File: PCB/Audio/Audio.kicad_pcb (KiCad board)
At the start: 2 copper layers, 70 x 70 mm, 36 parts, among them J1 JST-PH-SM4-TB, J3 TC2030-USB-NL-DS, J4 TF_PUSH, J5 USB-C-Socket-H, Q2 CJ2301, SW1 SW_Push, U1 R, U2 L, U3 TP4054, U4 ME6211C33M5G-N, U6 ESP32-S3-MINI-1

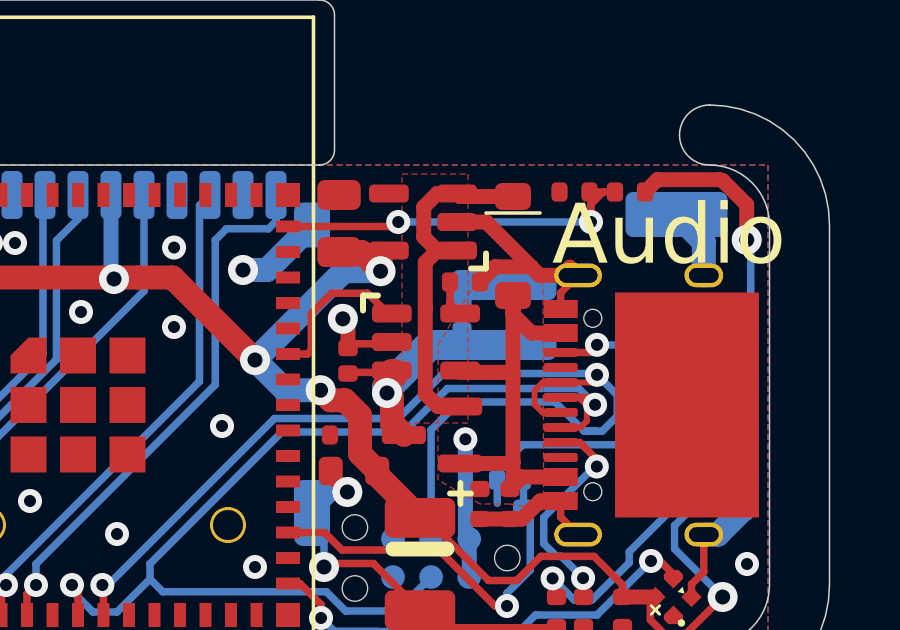
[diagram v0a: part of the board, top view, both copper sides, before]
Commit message: Cap clash moved
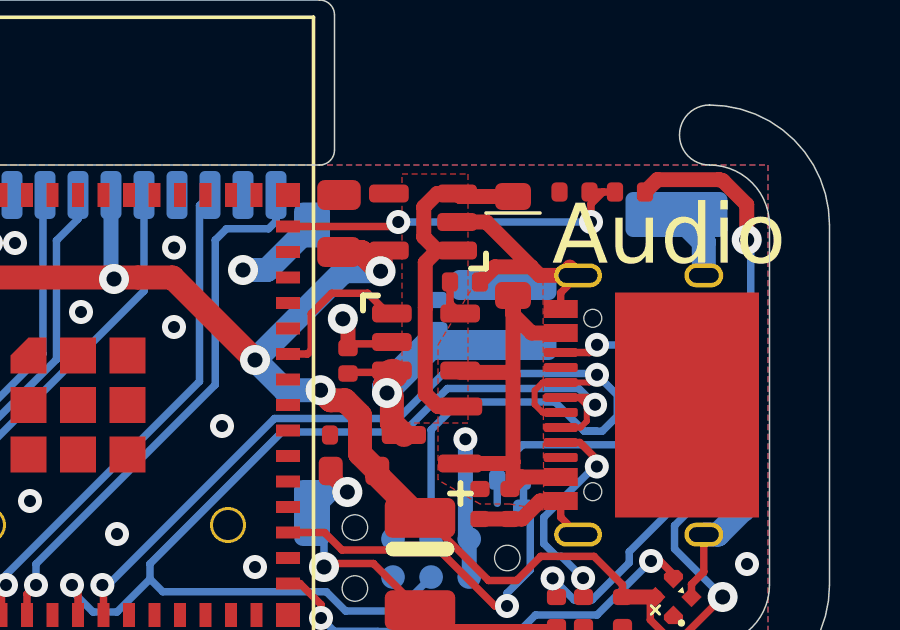
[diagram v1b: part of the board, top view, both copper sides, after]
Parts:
- moved C7 0.80 mm to (112.0, 97.0)

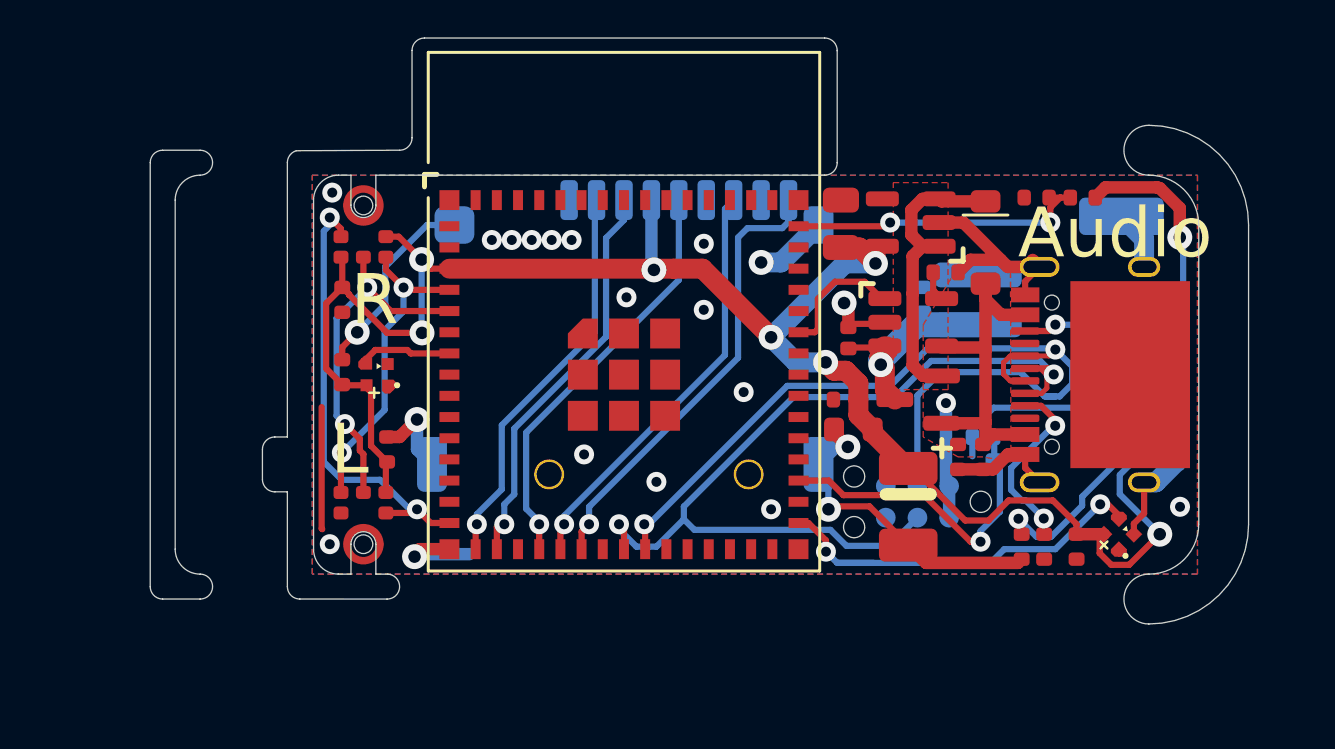
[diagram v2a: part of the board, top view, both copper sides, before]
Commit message: Rework, and pull ups
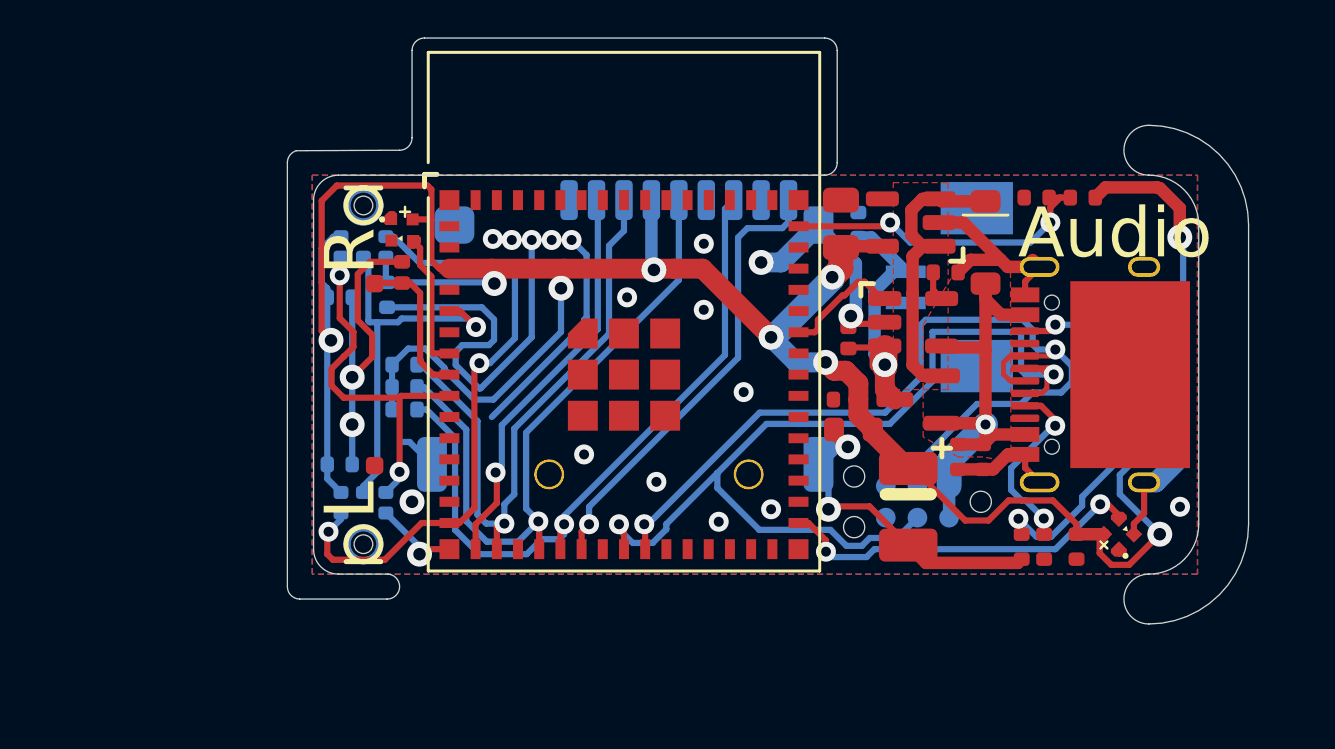
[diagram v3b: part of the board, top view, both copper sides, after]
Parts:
- added R3: 10K, RevK:R_0402, B.Cu at (91.2, 100.5)
- added R4: 10K, RevK:R_0402, B.Cu at (91.2, 99.6)
- added R7: 10K, RevK:R_0402, B.Cu at (91.2, 101.4)
- C13, C6, C8, U1, U2: moved to B.Cu
- D4, SW1: moved to F.Cu
- J1: value JST-PH-SM4-TB -> Battery; footprint RevK:JST_PH_S2B-PH-SM4-TB_1x02-1MP_P2.00mm_Horizontal -> RevK:1.25T-2PWT (Molex 532610271)
- moved SW1 28.7 mm to (90.0, 100.0), turned to 90 degrees
- moved D4 24.2 mm to (91.1, 95.9), turned to 90 degrees
- moved D5 5.89 mm to (91.1, 94.2), turned to 0 degrees
- moved C7 3.97 mm to (109.4, 94.0)
- moved C6 3.58 mm to (90.5, 96.8), turned to -90 degrees
- moved J1 2.89 mm to (114.2, 96.5), turned to 90 degrees
- moved C13 1.99 mm to (88.6, 103.6), turned to 180 degrees
- moved C8 0.14 mm to (88.6, 96.9), turned to 180 degrees
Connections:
- U6 pad 33: BUTTON -> unconnected-(U6-GPIO37-Pad33)
- U6 pad 4: WS -> unconnected-(U6-GPIO0-Pad4)
- U6 pad 8: unconnected-(U6-GPIO4-Pad8) -> BUTTON
- U6 pad 9: unconnected-(U6-GPIO5-Pad9) -> WS
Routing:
- net +3V3: track 97.9 -> 118.9 mm, vias 8 -> 9
- net GND: track 64.8 -> 81.3 mm
- net SDMISO: track 16.9 -> 28.1 mm
- net SDSCK: track 16.8 -> 26.7 mm
- net SDMOSI: track 16.0 -> 24.3 mm
- net SCK: track 17.9 -> 24.8 mm
- net BUTTON: track 12.9 -> 6.14 mm, vias 1 -> 0
- net VBAT: track 9.35 -> 11.8 mm
- net D-: track 36.6 -> 39.1 mm
- net WS: track 12.6 -> 14.8 mm
- net D+: track 38.7 -> 36.7 mm
- net BLINK2: track 3.68 -> 5.52 mm
- net BLINK: track 16.3 -> 14.7 mm
- net SD: track 14.1 -> 15.6 mm, vias 2 -> 1
- net VBUS: track 19.1 -> 19.7 mm
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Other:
- board text added: "+"
- board text added: "-"
- board text added: "BA"
- board text removed: "A"

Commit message: Placement
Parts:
- moved J1 1.75 mm to (112.5, 96.5)
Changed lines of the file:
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@@
 		(fp_arc
 			(start 0.27561 0.422802)
-			(mid 0.162324 0.224752)
+			(mid 0.162323 0.224752)
 			(end 0.123007 0.000003)
 			(stroke
@@
 		(fp_arc
 			(start 0.362198 -0.50939)
-			(mid 0.560248 -0.622677)
+			(mid 0.560248 -0.622676)
 			(end 0.784997 -0.661993)
 			(stroke
@@
 		(fp_arc
 			(start 0.362198 -0.50939)
-			(mid 0.560248 -0.622677)
+			(mid 0.560248 -0.622676)
 			(end 0.784997 -0.661993)
 			(stroke
@@
 		(fp_arc
 			(start 0.27561 0.422802)
-			(mid 0.162324 0.224752)
+			(mid 0.162323 0.224752)
 			(end 0.123007 0.000003)
 			(stroke
@@
 	(footprint "RevK:1.25T-2PWT (Molex 532610271)"
 		(layer "B.Cu")
-		(at 114.2 96.5 90)
+		(at 112.45 96.5 90)
 		(property "Reference" "J1"
 			(at 0 0 -90)
@@
 		(attr smd)
 		(pad "" smd rect
-			(at -3.157 -0.05 90)
+			(at -3.157 1.7 90)
 			(size 2.1 2.9)
 			(layers "B.Cu" "B.Paste" "B.Mask")
-			(teardrops
-				(best_length_ratio 0.5)
-				(max_length 1)
-				(best_width_ratio 1)
-				(max_width 2)
-				(curve_points 5)
-				(filter_ratio 0.9)
-				(enabled yes)
-				(allow_two_segments yes)
-				(prefer_zone_connections no)
-			)
 		)
 		(pad "" smd rect
-			(at 3.175 -0.05 90)
+			(at 3.175 1.7 90)
 			(size 2.1 2.9)
 			(layers "B.Cu" "B.Paste" "B.Mask")
-			(teardrops
-				(best_length_ratio 0.5)
-				(max_length 1)
-				(best_width_ratio 1)
-				(max_width 2)
-				(curve_points 5)
-				(filter_ratio 0.9)
-				(enabled yes)
-				(allow_two_segments yes)
-				(prefer_zone_connections no)
-			)
 		)
 		(pad "1" smd rect
-			(at -0.625 -2.9 90)
+			(at -0.625 -1.15 90)
 			(size 0.5 1.6)
 			(layers "B.Cu" "B.Paste" "B.Mask")
@@
 			(pinfunction "Pin_1")
 			(pintype "passive")
-			(teardrops
-				(best_length_ratio 0.5)
-				(max_length 1)
-				(best_width_ratio 1)
-				(max_width 2)
-				(curve_points 5)
-				(filter_ratio 0.9)
-				(enabled yes)
-				(allow_two_segments yes)
-				(prefer_zone_connections no)
-			)
 		)
 		(pad "2" smd rect
-			(at 0.625 -2.9 90)
+			(at 0.625 -1.15 90)
 			(size 0.5 1.6)
 			(layers "B.Cu" "B.Paste" "B.Mask")
@@
 			(pinfunction "Pin_2")
 			(pintype "passive")
-			(teardrops
-				(best_length_ratio 0.5)
-				(max_length 1)
-				(best_width_ratio 1)
-				(max_width 2)
-				(curve_points 5)
-				(filter_ratio 0.9)
-				(enabled yes)
-				(allow_two_segments yes)
-				(prefer_zone_connections no)
-			)
 		)
 		(model "${KISYS3DMOD}/Connector_Molex.3dshapes/Molex_PicoBlade_53261-0271_1x02-1MP_P1.25mm_Horizontal.step"
 			(offset
-				(xyz 0 -0.5 0)
+				(xyz 0 1.5 0)
 			)
 			(scale

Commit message: Resistors
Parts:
- removed R3, R4, R7: 10K, RevK:R_0402
- added R10: 10K, RevK:R_0402, B.Cu at (91.2, 101.8)
- added R11: 10K, RevK:R_0402, B.Cu at (91.2, 100.9)
- added R12: 10K, RevK:R_0402, B.Cu at (91.2, 100.0)
- added R13: 10K, RevK:R_0402, B.Cu at (91.2, 99.1)
- added R14: 10K, RevK:R_0402, B.Cu at (96.2, 92.7)
- added R9: 10K, RevK:R_0402, B.Cu at (108.8, 100.7)
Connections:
- J4 pad 1: unconnected-(J4-DAT2-Pad1) -> Net-(J4-DAT2)
- J4 pad 8: unconnected-(J4-DAT1-Pad8) -> Net-(J4-DAT1)
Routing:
- net Net-(J4-DAT1): track 0.00 -> 29.8 mm
- net GND: track 81.3 -> 68.8 mm, vias 22 -> 20
- net SDSS: track 16.1 -> 21.1 mm
- net +3V3: track 118.9 -> 123.6 mm, vias 9 -> 10
- net SDMISO: track 28.1 -> 30.2 mm
- net Net-(J4-DAT2): track 0.00 -> 1.18 mm

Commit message: Reworked
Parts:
- moved R9 17.6 mm to (91.2, 101.9), turned to 0 degrees
- moved D5 7.72 mm to (86.0, 100.0)
- moved C13 1.72 mm to (87.6, 102.2), turned to -90 degrees
- moved C8 1.28 mm to (87.6, 97.7), turned to 90 degrees
- moved U2 1.08 mm to (89.4, 104.9), turned to -45 degrees
- moved U1 1.06 mm to (89.4, 95.1), turned to 45 degrees
- moved C6 0.92 mm to (91.2, 97.4), turned to 0 degrees
- moved R11 0.80 mm to (91.2, 100.1)
- moved R10 0.80 mm to (91.2, 101.0)
- moved R12 0.80 mm to (91.2, 99.2)
- moved R13 0.80 mm to (91.2, 98.3)
- moved D4 0.14 mm to (91.0, 96.0), turned to -90 degrees
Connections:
- U6 pad 10: unconnected-(U6-GPIO6-Pad10) -> WS
- U6 pad 11: unconnected-(U6-GPIO7-Pad11) -> SD
- U6 pad 12: unconnected-(U6-GPIO8-Pad12) -> GND
- U6 pad 13: unconnected-(U6-GPIO9-Pad13) -> BLINK2
- U6 pad 14: unconnected-(U6-GPIO10-Pad14) -> SCK
- U6 pad 15: SCK -> GND
- U6 pad 22: unconnected-(U6-GPIO18-Pad22) -> CHARGING
- U6 pad 5: SD -> BUTTON
- U6 pad 6: unconnected-(U6-GPIO2-Pad6) -> GND
- U6 pad 7: BLINK2 -> unconnected-(U6-GPIO3-Pad7)
- U6 pad 8: BUTTON -> unconnected-(U6-GPIO4-Pad8)
- U6 pad 9: WS -> unconnected-(U6-GPIO5-Pad9)
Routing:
- net CHARGING: track 4.75 -> 19.0 mm
- net SCK: track 24.6 -> 30.2 mm
- net BLINK2: track 5.52 -> 10.5 mm
- net +3V3: track 123.6 -> 119.0 mm, vias 10 -> 8
- net GND: track 68.8 -> 72.4 mm, vias 20 -> 23
- net WS: track 14.8 -> 16.8 mm, vias 2 -> 1
- net BUTTON: track 6.11 -> 4.45 mm
- net SDSS: track 21.1 -> 22.3 mm
- net SDMISO: track 30.2 -> 31.3 mm
- net SDSCK: track 26.3 -> 27.4 mm
- net Net-(J4-DAT1): track 29.8 -> 29.0 mm
- net SDMOSI: track 24.0 -> 24.9 mm
- net D-: track 39.3 -> 38.7 mm
- net SDCD: track 18.0 -> 17.4 mm
- net SD: track 15.5 -> 15.1 mm, vias 1 -> 2
